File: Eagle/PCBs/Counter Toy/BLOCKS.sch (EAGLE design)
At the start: 16 parts, among them Q1 2N7002, Q5 2N7002, Q6 2N7002, Q9 2N7002, U2 TL072D

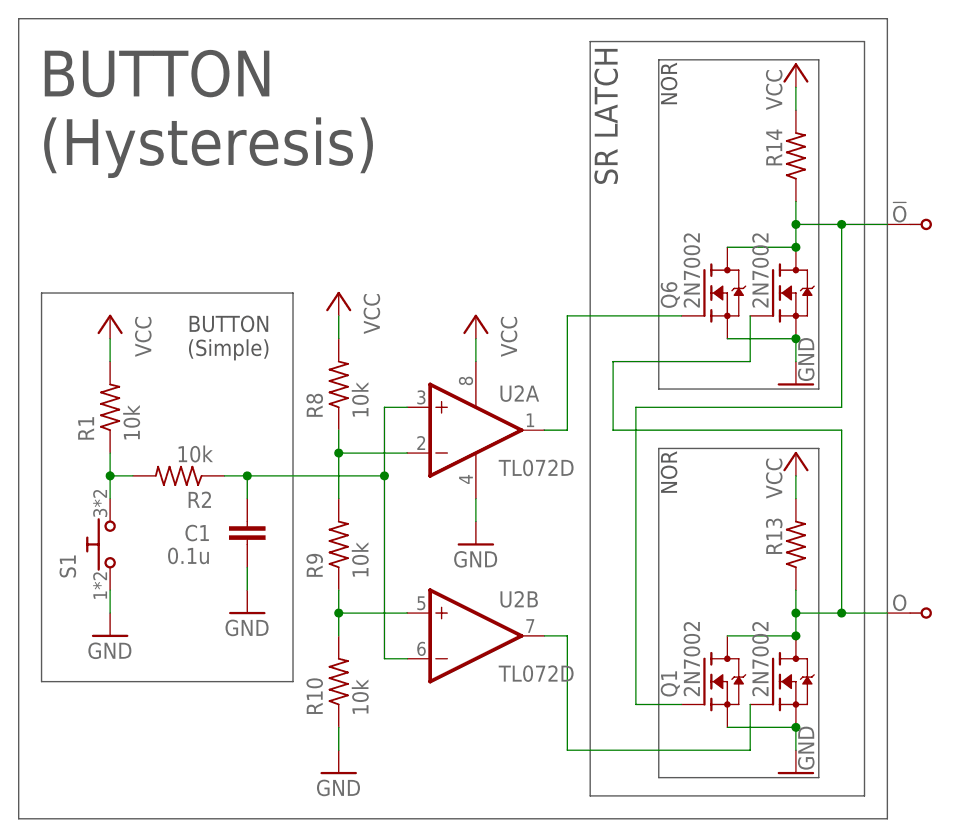
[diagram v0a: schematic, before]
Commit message: Gave in and used a read schmitt trigger on my buttons
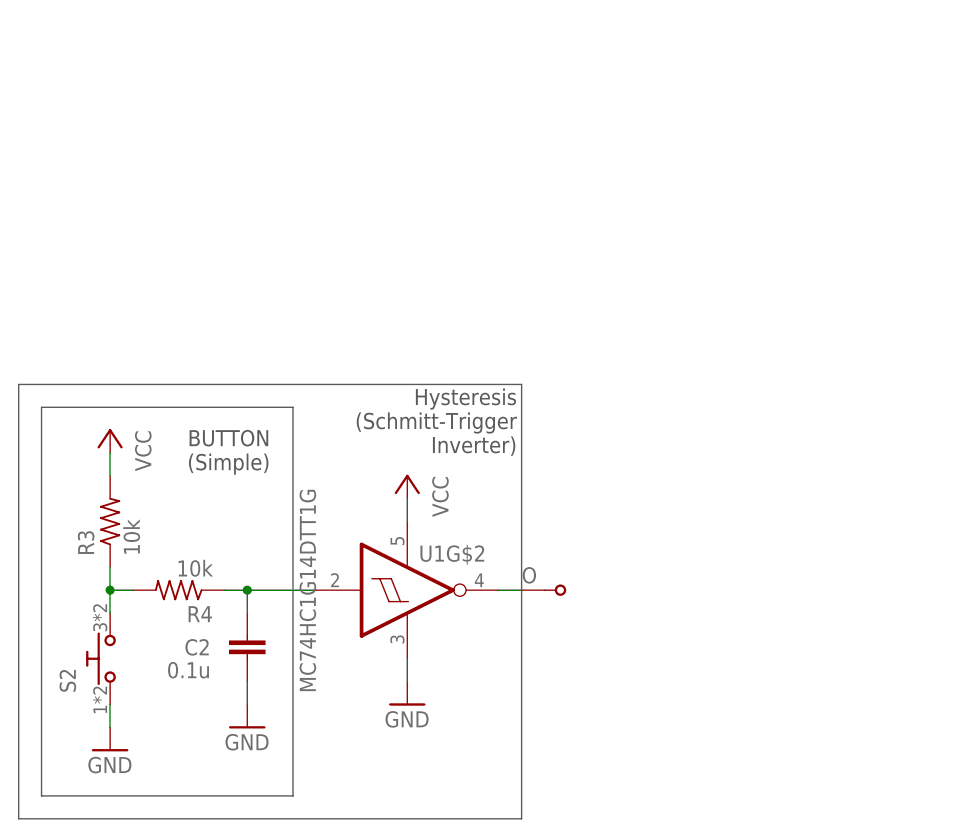
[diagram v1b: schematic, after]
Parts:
- removed !O: TPPAD6, ellajameson-core:TPPAD6
- removed C1: 0.1u, ellajameson-core:CAP0603
- removed Q1, Q5, Q6, Q9: 2N7002, ellajameson-core:2N7002
- removed R1, R10, R2, R8, R9: 10k, ellajameson-core:RES0603
- removed R13, R14: (no value), ellajameson-core:RES0603
- removed S1: (no value), ellajameson-core:SWITCH-NO-MOMPTS815SJM250SMTRLFS
- removed U2: TL072D, ellajameson-core:TL072D
- added C2: 0.1u, ellajameson-core:CAP0603
- added R3, R4: 10k, ellajameson-core:RES0603
- added S2: (no value), ellajameson-core:SWITCH-NO-MOMPTS815SJM250SMTRLFS
- added U1: MC74HC1G14DTT1G, ellajameson-core:MC74HC1G14DTT1G
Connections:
- removed net N$13: Q5.G, U2B.OUT
- removed net N$14: O.S, Q1.D, Q5.D, Q9.G, R13.1
- removed net N$15: Q6.G, U2A.OUT
- removed net N$16: !O.S, Q1.G, Q6.D, Q9.D, R14.1
- removed net N$6: R10.2, R9.1, U2B.+IN
- removed net N$7: R8.1, R9.2, U2A.-IN
- removed net N$8: C1.1, R2.1, U2A.+IN, U2B.-IN
- new net N$1: O.S, U1G$2.O
- new net N$3: R3.1, R4.2, S2.S
- net GND: now also C2.2, S2.P, U1G$1.V-; no longer C1.2, Q1.S, Q5.S, Q6.S, Q9.S, R10.1, S1.P, U2P.V-
- net N$4: now also C2.1, R4.1, U1G$2.I; no longer R1.1, R2.2, S1.S
- net VCC: now also R3.2, U1G$1.V+; no longer R1.2, R13.2, R14.2, R8.2, U2P.V+
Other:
- note added: "Hysteresis (Schmitt-Trigger Inverter)"
- note removed: "BUTTON (Hysteresis)"
- note removed: "NOR"
- note removed: "SR LATCH"
- moved on the sheet: O

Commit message: Better DFF
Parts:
- removed C2: 0.1u, ellajameson-core:CAP0603
- removed O: TPPAD6, ellajameson-core:TPPAD6
- removed S2: (no value), ellajameson-core:SWITCH-NO-MOMPTS815SJM250SMTRLFS
- removed U1: MC74HC1G14DTT1G, ellajameson-core:MC74HC1G14DTT1G
- added !Q, !R, CLK, D, Q: TPPAD6, ellajameson-core:TPPAD6
- added Q10, Q11, Q12, Q15, Q16, Q17, Q2, Q21, Q22, Q23, Q4, Q5, Q6, Q7, Q8, Q9: 2N7002, ellajameson-core:2N7002
- added R1, R5, R6, R8: (no value), ellajameson-core:RES0603
- R3, R4: value 10k -> (none)
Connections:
- removed net N$1: O.S, U1G$2.O
- removed net N$3: R3.1, R4.2, S2.S
- new net N$10: Q2.S, Q5.D
- new net N$12: Q5.S, Q6.D
- new net N$14: Q4.S, Q7.D
- new net N$16: Q21.G, Q8.D, R5.1
- new net N$18: Q17.G, Q8.G, Q9.D, R4.1
- new net N$19: D.S, Q10.G
- new net N$20: Q10.D, Q9.S
- new net N$22: Q10.S, Q11.D
- new net N$24: Q12.D, Q8.S
- new net N$31: CLK.S, Q16.G, Q22.G
- new net N$32: Q15.S, Q16.D
- new net N$34: Q16.S, Q17.D
- new net N$44: Q21.S, Q22.D
- new net N$45: !R.S, Q11.G, Q23.G, Q6.G
- new net N$46: Q22.S, Q23.D
- new net N$7: Q12.G, Q15.G, Q21.D, Q4.G, R8.1
- new net N$8: Q.S, Q2.G, Q4.D, R3.1
- new net N$9: Q15.D, Q5.G, Q9.G, R6.1
- net GND: now also Q11.S, Q12.S, Q17.S, Q23.S, Q6.S, Q7.S; no longer C2.2, S2.P, U1G$1.V-
- net N$4: now also !Q.S, Q2.D, Q7.G, R1.1; no longer C2.1, R4.1, U1G$2.I
- net VCC: now also R1.2, R4.2, R5.2, R6.2, R8.2; no longer U1G$1.V+
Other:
- note added: "DFF"
- note added: "NAND"
- note added: "NAND3"
- note removed: "BUTTON (Simple)"
- note removed: "Hysteresis (Schmitt-Trigger Inverter)"
- moved on the sheet: R3, R4

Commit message: Testing open collector setup
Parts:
- removed !Q, !R, CLK, D, Q: TPPAD6, ellajameson-core:TPPAD6
- removed Q10, Q11, Q12, Q15, Q16, Q17, Q2, Q21, Q22, Q23, Q4, Q5, Q6, Q7, Q8, Q9: 2N7002, ellajameson-core:2N7002
- removed R3, R4, R5, R6, R8: (no value), ellajameson-core:RES0603
- added D1: (no value), ellajameson-core:LED0603
- added DRAINA1, DRAINB1, DRAINC1, DRAIND1, GATE1, SOURCEA1, SOURCEB1, SOURCEC1, SOURCED1: TPWIRE, ellajameson-core:TPWIRE
- added JD1, JN1, JP1, JS1: SJ_NO, ellajameson-core:SJ_NO
- added Q1: 2N7002, ellajameson-core:2N7002
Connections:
- removed net N$10: Q2.S, Q5.D
- removed net N$12: Q5.S, Q6.D
- removed net N$14: Q4.S, Q7.D
- removed net N$16: Q21.G, Q8.D, R5.1
- removed net N$18: Q17.G, Q8.G, Q9.D, R4.1
- removed net N$19: D.S, Q10.G
- removed net N$20: Q10.D, Q9.S
- removed net N$22: Q10.S, Q11.D
- removed net N$24: Q12.D, Q8.S
- removed net N$31: CLK.S, Q16.G, Q22.G
- removed net N$32: Q15.S, Q16.D
- removed net N$34: Q16.S, Q17.D
- removed net N$4: !Q.S, Q2.D, Q7.G, R1.1
- removed net N$44: Q21.S, Q22.D
- removed net N$45: !R.S, Q11.G, Q23.G, Q6.G
- removed net N$46: Q22.S, Q23.D
- removed net N$9: Q15.D, Q5.G, Q9.G, R6.1
- new net N$5: D1.A, JP1.2, R1.1
- new net N$6: D1.K, DRAINA1.S, DRAINB1.S, DRAINC1.S, DRAIND1.S, JD1.2, JP1.1, Q1.D
- net GND: now also JN1.1; no longer Q11.S, Q12.S, Q17.S, Q23.S, Q6.S, Q7.S
- net N$7: now also JN1.2, JS1.2, Q1.S, SOURCEA1.S, SOURCEB1.S, SOURCEC1.S, SOURCED1.S; no longer Q12.G, Q15.G, Q21.D, Q4.G, R8.1
- net N$8: now also GATE1.S, Q1.G; no longer Q.S, Q2.G, Q4.D, R3.1
- net VCC: no longer R3.2, R4.2, R5.2, R6.2, R8.2
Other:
- note added: "NMOS Logic Transistor Cell"
- note removed: "DFF"
- note removed: "NAND"
- note removed: "NAND3"
- moved on the sheet: R1
